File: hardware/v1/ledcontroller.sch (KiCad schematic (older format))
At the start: 4 parts, among them U2 MAX7221

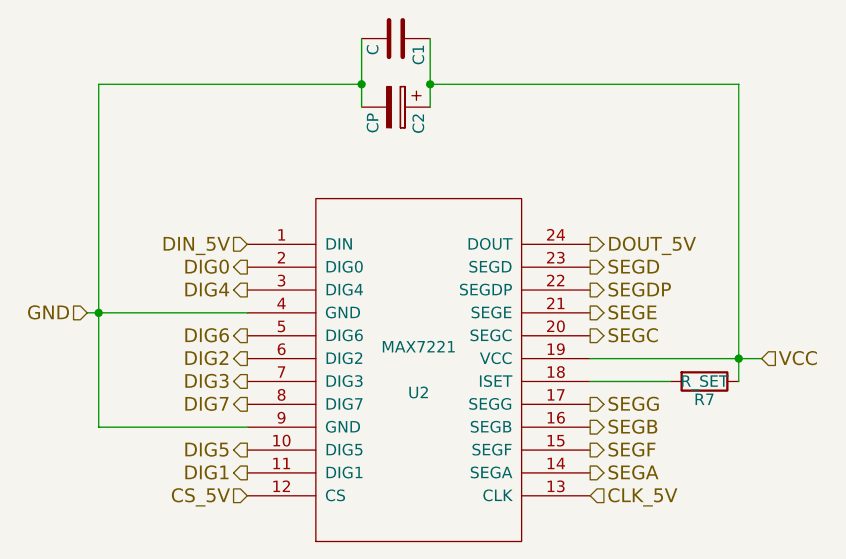
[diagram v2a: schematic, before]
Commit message: Complete piconnect circuit and start routing.
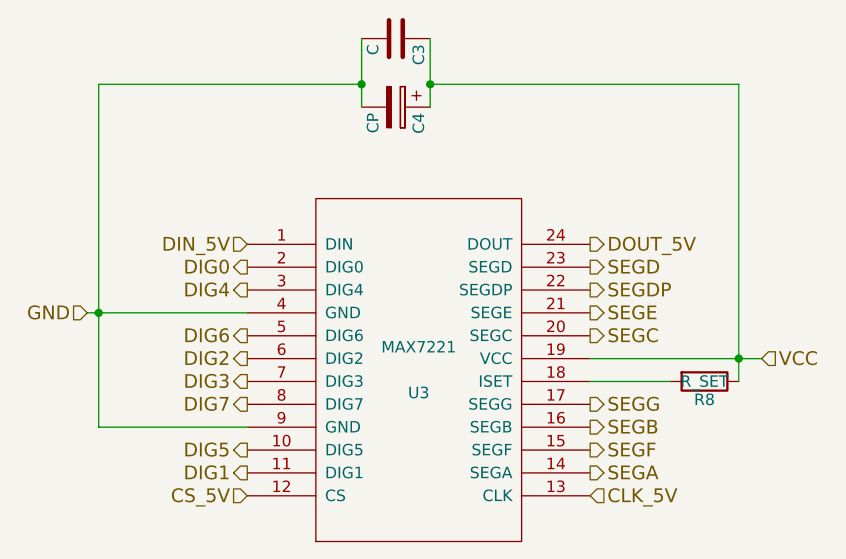
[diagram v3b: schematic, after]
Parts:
- C2: footprint Discret:CP36V -> Capacitors_ThroughHole:C_Radial_D5_L11_P2
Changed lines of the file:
@@
 AR Path="/57A5CF2B/57A34228" Ref="U2"  Part="1"
 AR Path="/57A5D8B0/57A34228" Ref="U3"  Part="1"
-F 0 "U2" H 5750 3500 50  0000 C CNN
+F 0 "U3" H 5750 3500 50  0000 C CNN
 F 1 "MAX7221" H 5750 3700 50  0000 C CNN
 F 2 "DIL24:DIL24" H 5750 3600 50  0001 C CNN
@@
 AR Path="/57A5CF2B/57A343D9" Ref="R7"  Part="1"
 AR Path="/57A5D8B0/57A343D9" Ref="R8"  Part="1"
-F 0 "R7" V 7080 3650 50  0000 C CNN
+F 0 "R8" V 7080 3650 50  0000 C CNN
 F 1 "R_SET" V 7000 3650 50  0000 C CNN
 F 2 "Resistors_ThroughHole:Resistor_Horizontal_RM10mm" V 6930 3650 50  0001 C CNN
@@
 AR Path="/57A5CF2B/57A3585E" Ref="C1"  Part="1"
 AR Path="/57A5D8B0/57A3585E" Ref="C3"  Part="1"
-F 0 "C1" H 5675 2250 50  0000 L CNN
+F 0 "C3" H 5675 2250 50  0000 L CNN
 F 1 "C" H 5675 2050 50  0000 L CNN
 F 2 "Capacitors_ThroughHole:C_Disc_D6_P5" H 5688 2000 50  0001 C CNN
@@
 AR Path="/57A5CF2B/57A358C3" Ref="C2"  Part="1"
 AR Path="/57A5D8B0/57A358C3" Ref="C4"  Part="1"
-F 0 "C2" H 5675 2550 50  0000 L CNN
+F 0 "C4" H 5675 2550 50  0000 L CNN
 F 1 "CP" H 5675 2350 50  0000 L CNN
-F 2 "Discret:CP36V" H 5688 2300 50  0001 C CNN
+F 2 "Capacitors_ThroughHole:C_Radial_D5_L11_P2" H 5688 2300 50  0001 C CNN
 F 3 "" H 5650 2450 50  0000 C CNN
 	1    5650 2450

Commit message: Add mosfet clock gates to I2C connector rows - because addresses conflict and the second bus (I2C0) cannot be used safely on the raspberry pi.
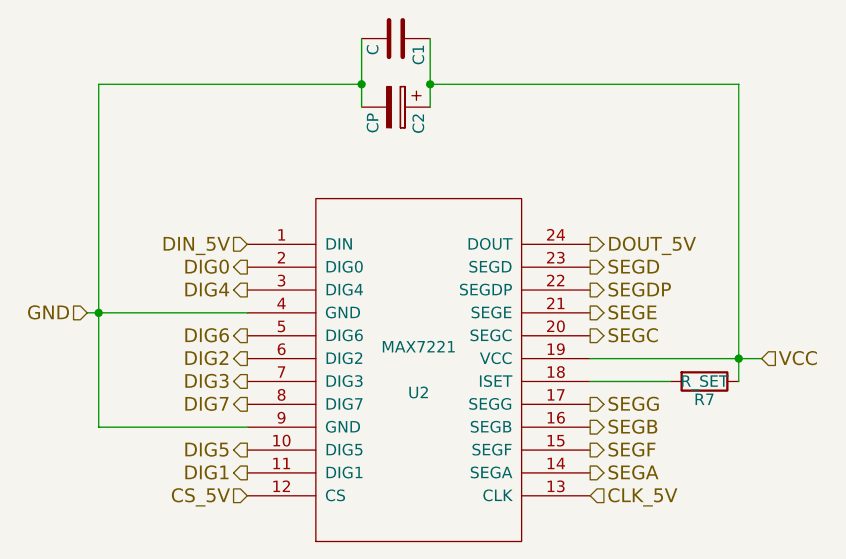
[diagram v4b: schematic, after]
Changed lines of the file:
@@
 LIBS:contrib
 LIBS:valves
-LIBS:Pi2_Connector
-LIBS:MAX7221
-LIBS:MCP23S17
-LIBS:MCP23017
 LIBS:piconnect-cache
 EELAYER 25 0
@@
 AR Path="/57A5CF2B/57A34228" Ref="U2"  Part="1"
 AR Path="/57A5D8B0/57A34228" Ref="U3"  Part="1"
-F 0 "U3" H 5750 3500 50  0000 C CNN
+F 0 "U2" H 5750 3500 50  0000 C CNN
 F 1 "MAX7221" H 5750 3700 50  0000 C CNN
 F 2 "DIL24:DIL24" H 5750 3600 50  0001 C CNN
@@
 AR Path="/57A5CF2B/57A343D9" Ref="R7"  Part="1"
 AR Path="/57A5D8B0/57A343D9" Ref="R8"  Part="1"
-F 0 "R8" V 7080 3650 50  0000 C CNN
+F 0 "R7" V 7080 3650 50  0000 C CNN
 F 1 "R_SET" V 7000 3650 50  0000 C CNN
 F 2 "Resistors_ThroughHole:Resistor_Horizontal_RM10mm" V 6930 3650 50  0001 C CNN
@@
 AR Path="/57A5CF2B/57A3585E" Ref="C1"  Part="1"
 AR Path="/57A5D8B0/57A3585E" Ref="C3"  Part="1"
-F 0 "C3" H 5675 2250 50  0000 L CNN
+F 0 "C1" H 5675 2250 50  0000 L CNN
 F 1 "C" H 5675 2050 50  0000 L CNN
 F 2 "Capacitors_ThroughHole:C_Disc_D6_P5" H 5688 2000 50  0001 C CNN
@@
 AR Path="/57A5CF2B/57A358C3" Ref="C2"  Part="1"
 AR Path="/57A5D8B0/57A358C3" Ref="C4"  Part="1"
-F 0 "C4" H 5675 2550 50  0000 L CNN
+F 0 "C2" H 5675 2550 50  0000 L CNN
 F 1 "CP" H 5675 2350 50  0000 L CNN
 F 2 "Capacitors_ThroughHole:C_Radial_D5_L11_P2" H 5688 2300 50  0001 C CNN
